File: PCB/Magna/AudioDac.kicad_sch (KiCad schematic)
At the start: 20 parts, among them U501 CS4344, U602 NE5532

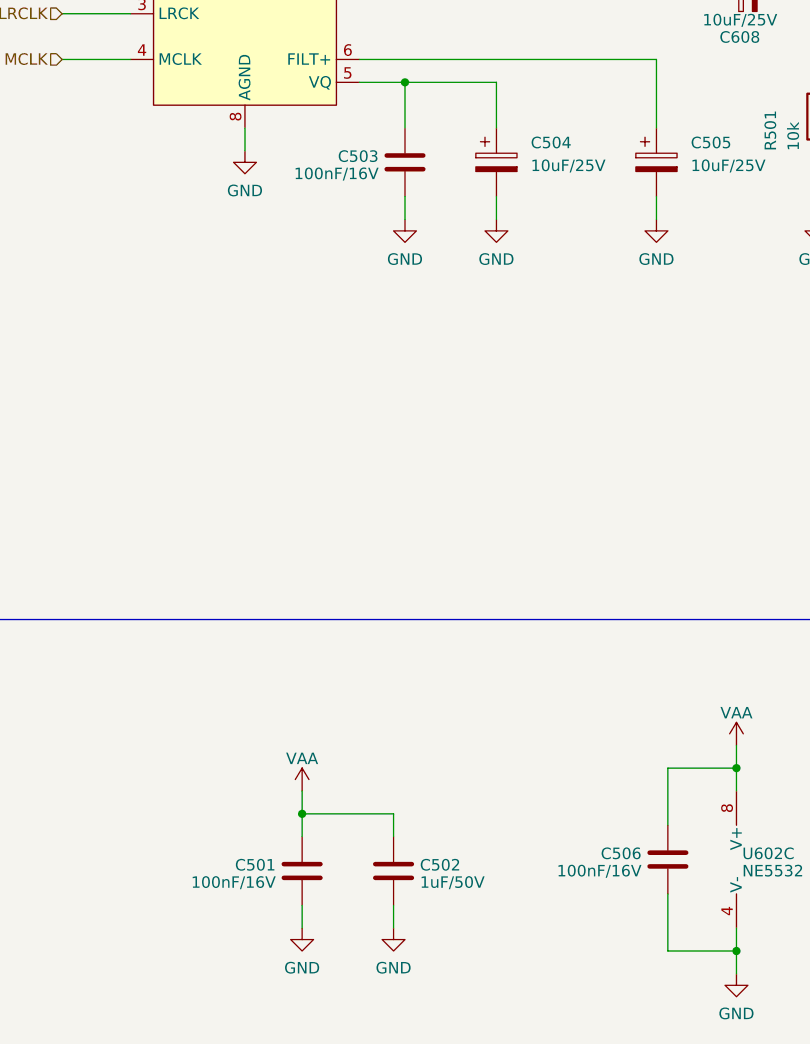
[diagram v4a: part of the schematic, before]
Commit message: Add even more component footprints and partnumbers
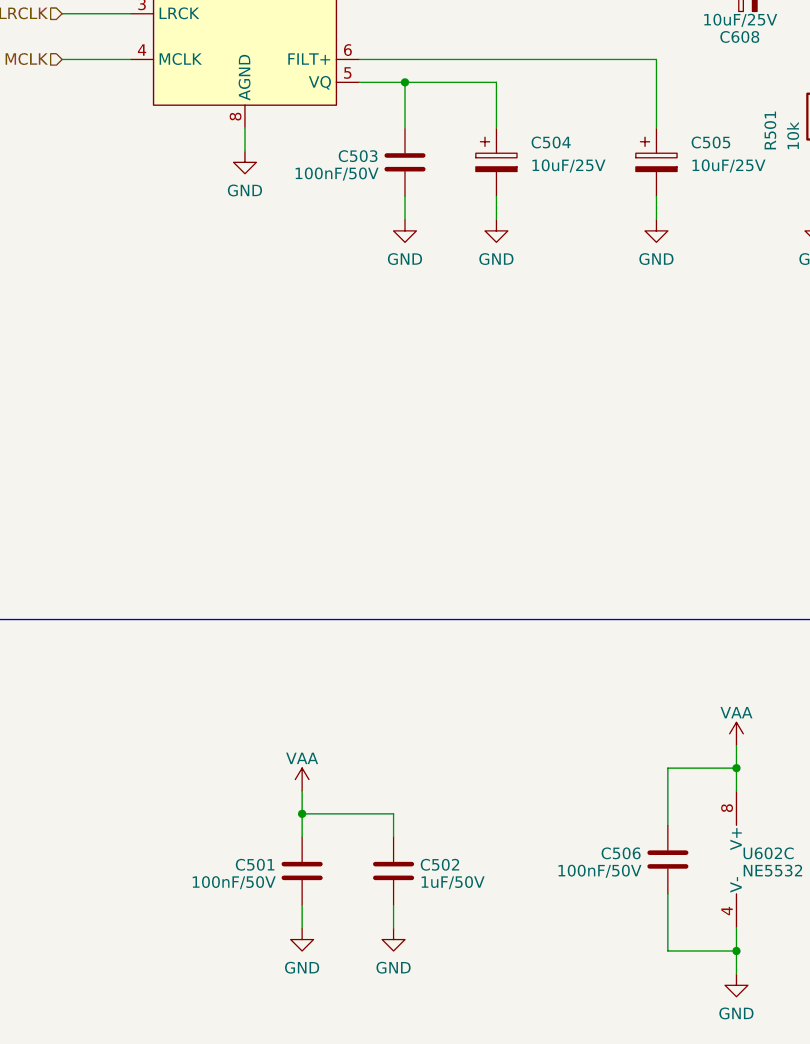
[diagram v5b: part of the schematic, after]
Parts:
- C501, C503, C506: value 100nF/16V -> 100nF/50V; footprint Capacitor_SMD:C_0805_2012Metric -> Capacitor_SMD:C_0805_2012Metric_Pad1.18x1.45mm_HandSolder; LCSC C218638 -> C49678
- C502, C509, C510: footprint Capacitor_SMD:C_0805_2012Metric -> Capacitor_SMD:C_0805_2012Metric_Pad1.18x1.45mm_HandSolder
- R501, R502, R505, R506: footprint Resistor_SMD:R_0805_2012Metric -> Resistor_SMD:R_0805_2012Metric_Pad1.20x1.40mm_HandSolder
- U602: footprint (none) -> Package_SO:SOIC-8_3.9x4.9mm_P1.27mm
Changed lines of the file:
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@@
       (effects (font (size 1.27 1.27)) (justify right))
     )
-    (property "Footprint" "Resistor_SMD:R_0805_2012Metric" (at 224.028 53.34 90)
+    (property "Footprint" "Resistor_SMD:R_0805_2012Metric_Pad1.20x1.40mm_HandSolder" (at 224.028 53.34 90)
       (effects (font (size 1.27 1.27)) hide)
     )
@@
       (effects (font (size 1.27 1.27)) (justify left))
     )
-    (property "Footprint" "Capacitor_SMD:C_0805_2012Metric" (at 82.2452 171.45 0)
+    (property "Footprint" "Capacitor_SMD:C_0805_2012Metric_Pad1.18x1.45mm_HandSolder" (at 82.2452 171.45 0)
       (effects (font (size 1.27 1.27)) hide)
     )
@@
       (effects (font (size 1.27 1.27)) (justify left))
     )
-    (property "Value" "100nF/16V" (at 108.839 167.6473 0)
-      (effects (font (size 1.27 1.27)) (justify left))
-    )
-    (property "Footprint" "Capacitor_SMD:C_0805_2012Metric" (at 110.7948 170.18 0)
+    (property "Value" "100nF/50V" (at 108.839 167.6473 0)
+      (effects (font (size 1.27 1.27)) (justify left))
+    )
+    (property "Footprint" "Capacitor_SMD:C_0805_2012Metric_Pad1.18x1.45mm_HandSolder" (at 110.7948 170.18 0)
       (effects (font (size 1.27 1.27)) hide)
     )
@@
       (effects (font (size 1.27 1.27)) hide)
     )
-    (property "LCSC" "C218638" (at 111.76 166.37 0)
+    (property "LCSC" "C49678" (at 111.76 166.37 0)
       (effects (font (size 1.27 1.27)) hide)
     )
@@
       (effects (font (size 1.27 1.27)) (justify left))
     )
-    (property "Footprint" "Resistor_SMD:R_0805_2012Metric" (at 130.048 83.82 90)
+    (property "Footprint" "Resistor_SMD:R_0805_2012Metric_Pad1.20x1.40mm_HandSolder" (at 130.048 83.82 90)
       (effects (font (size 1.27 1.27)) hide)
     )
@@
       (effects (font (size 1.27 1.27)) (justify right))
     )
-    (property "Footprint" "Resistor_SMD:R_0805_2012Metric" (at 213.868 53.34 90)
+    (property "Footprint" "Resistor_SMD:R_0805_2012Metric_Pad1.20x1.40mm_HandSolder" (at 213.868 53.34 90)
       (effects (font (size 1.27 1.27)) hide)
     )
@@
       (effects (font (size 1.27 1.27)) (justify left))
     )
-    (property "Value" "100nF/16V" (at 79.629 90.1773 0)
-      (effects (font (size 1.27 1.27)) (justify left))
-    )
-    (property "Footprint" "Capacitor_SMD:C_0805_2012Metric" (at 81.5848 92.71 0)
+    (property "Value" "100nF/50V" (at 79.629 90.1773 0)
+      (effects (font (size 1.27 1.27)) (justify left))
+    )
+    (property "Footprint" "Capacitor_SMD:C_0805_2012Metric_Pad1.18x1.45mm_HandSolder" (at 81.5848 92.71 0)
       (effects (font (size 1.27 1.27)) hide)
     )
@@
       (effects (font (size 1.27 1.27)) hide)
     )
-    (property "LCSC" "C218638" (at 82.55 88.9 0)
+    (property "LCSC" "C49678" (at 82.55 88.9 0)
       (effects (font (size 1.27 1.27)) hide)
     )
@@
       (effects (font (size 1.27 1.27)) (justify left))
     )
-    (property "Footprint" "Capacitor_SMD:C_0805_2012Metric" (at 169.8752 87.63 0)
+    (property "Footprint" "Capacitor_SMD:C_0805_2012Metric_Pad1.18x1.45mm_HandSolder" (at 169.8752 87.63 0)
       (effects (font (size 1.27 1.27)) hide)
     )
@@
       (effects (font (size 1.27 1.27)))
     )
-    (property "Footprint" "" (at 245.11 90.17 0)
+    (property "Footprint" "Package_SO:SOIC-8_3.9x4.9mm_P1.27mm" (at 245.11 90.17 0)
       (effects (font (size 1.27 1.27)) hide)
     )
@@
       (effects (font (size 1.27 1.27)) (justify left))
     )
-    (property "Footprint" "Resistor_SMD:R_0805_2012Metric" (at 140.208 83.82 90)
+    (property "Footprint" "Resistor_SMD:R_0805_2012Metric_Pad1.20x1.40mm_HandSolder" (at 140.208 83.82 90)
       (effects (font (size 1.27 1.27)) hide)
     )
@@
       (effects (font (size 1.27 1.27)))
     )
-    (property "Footprint" "" (at 245.11 67.31 0)
+    (property "Footprint" "Package_SO:SOIC-8_3.9x4.9mm_P1.27mm" (at 245.11 67.31 0)
       (effects (font (size 1.27 1.27)) hide)
     )
@@
       (effects (font (size 1.27 1.27)) (justify left))
     )
-    (property "Footprint" "Capacitor_SMD:C_0805_2012Metric" (at 157.7848 87.63 0)
+    (property "Footprint" "Capacitor_SMD:C_0805_2012Metric_Pad1.18x1.45mm_HandSolder" (at 157.7848 87.63 0)
       (effects (font (size 1.27 1.27)) hide)
     )
@@
       (effects (font (size 1.27 1.27)) (justify left))
     )
-    (property "Value" "100nF/16V" (at 68.199 168.9173 0)
-      (effects (font (size 1.27 1.27)) (justify left))
-    )
-    (property "Footprint" "Capacitor_SMD:C_0805_2012Metric" (at 70.1548 171.45 0)
+    (property "Value" "100nF/50V" (at 68.199 168.9173 0)
+      (effects (font (size 1.27 1.27)) (justify left))
+    )
+    (property "Footprint" "Capacitor_SMD:C_0805_2012Metric_Pad1.18x1.45mm_HandSolder" (at 70.1548 171.45 0)
       (effects (font (size 1.27 1.27)) hide)
     )
@@
       (effects (font (size 1.27 1.27)) hide)
     )
-    (property "LCSC" "C218638" (at 71.12 167.64 0)
+    (property "LCSC" "C49678" (at 71.12 167.64 0)
       (effects (font (size 1.27 1.27)) hide)
     )
@@
       (effects (font (size 1.27 1.27)) (justify left))
     )
-    (property "Footprint" "" (at 121.92 166.37 0)
-      (effects (font (size 1.27 1.27)) hide)
-    )
+    (property "Footprint" "Package_SO:SOIC-8_3.9x4.9mm_P1.27mm" (at 121.92 166.37 0)
+      (effects (font (size 1.27 1.27)) hide)
+    )
